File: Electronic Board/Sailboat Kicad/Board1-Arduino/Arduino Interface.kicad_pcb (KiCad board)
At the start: 2 copper layers, 69.9 x 101 mm, 51 parts, among them J1 Conn_01x02, J10 Conn_01x02, J11 Conn_01x03_Male, J12 Conn_01x03_Male, J13 Conn_01x03_Male, J14 Conn_01x03_Male, J15 Conn_01x04, J16 Conn_01x04, J17 Conn_01x04, J18 Conn_01x04, J19 Conn_01x03, J2 Conn_01x08, J20 Conn_01x03, J21 Conn_01x02, J22 Conn_01x02, J23 Conn_01x06, J24 Conn_01x03, J25 Conn_01x06, J26 Conn_02x02_Odd_Even, J3 Conn_01x08, J31 Conn_01x04, J32 Conn_01x04, J34 Conn_01x02, J35 Conn_01x02, J36 Conn_01x02, J37 Conn_01x02, J4 Conn_01x08, J5 Conn_02x18_Odd_Even, J6 Conn_01x08, J7 Conn_01x08, J8 Conn_01x08, J9 Conn_01x02, U1 L7805, U2 L7805, U3 L7805

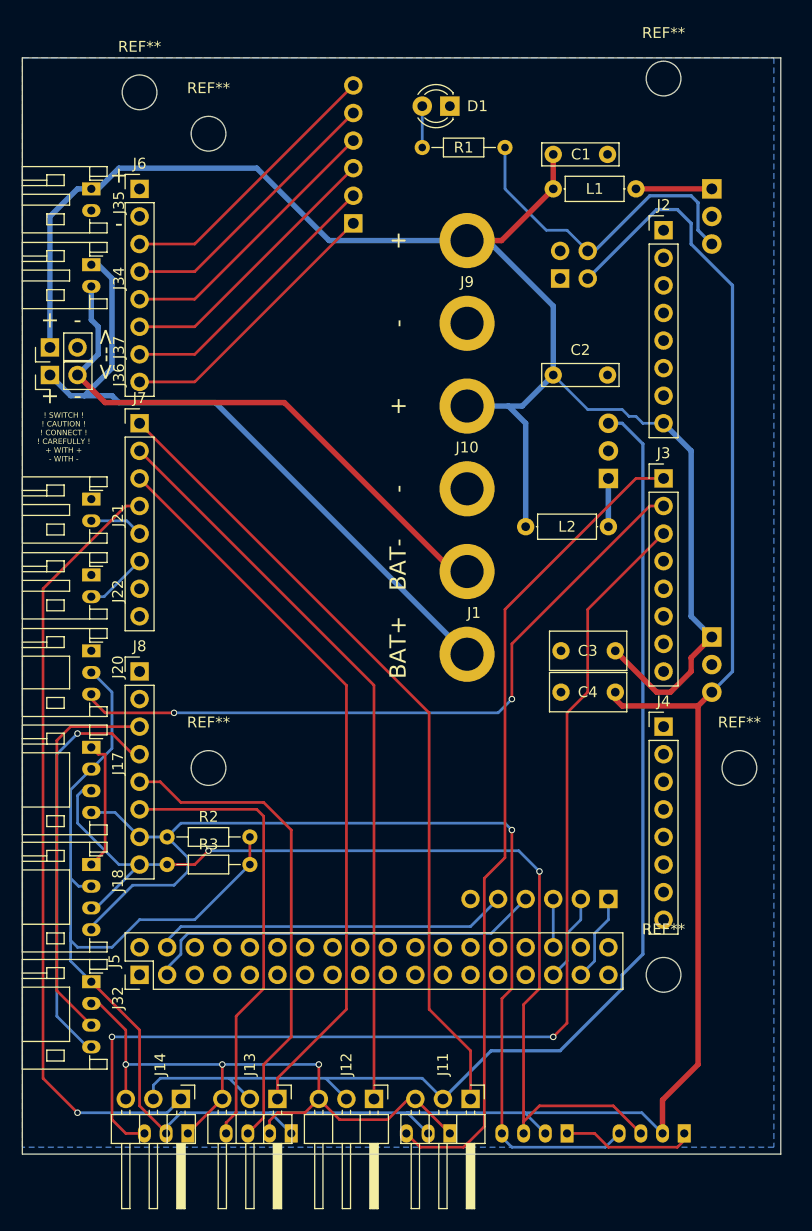
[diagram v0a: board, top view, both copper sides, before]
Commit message: Cleaned up, and added security, text and better usability, preparation for board v2
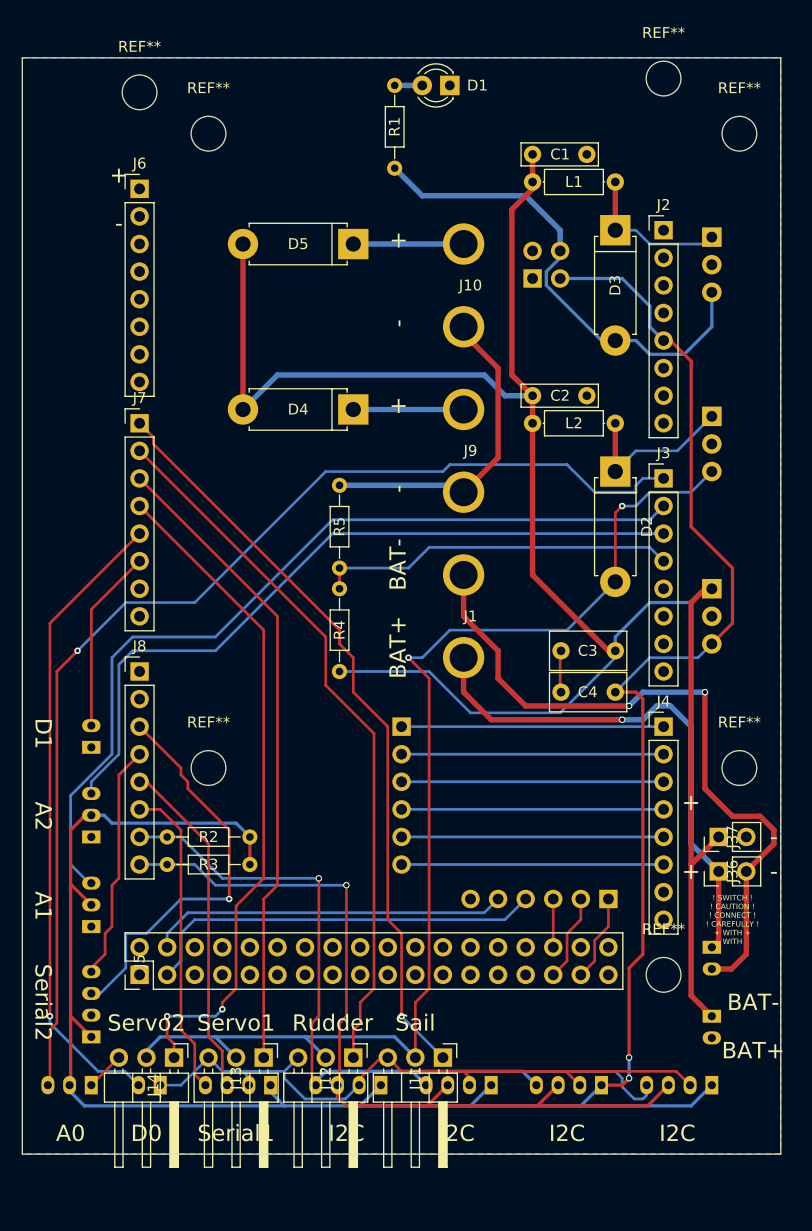
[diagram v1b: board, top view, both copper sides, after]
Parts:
- added D2: D_Schottky, Diodes_THT:D_5W_P10.16mm_Horizontal, F.Cu at (172.7, 90.8)
- added D3: D_Schottky, Diodes_THT:D_5W_P10.16mm_Horizontal, F.Cu at (172.7, 68.6)
- added D4: D_Schottky, Diodes_THT:D_5W_P10.16mm_Horizontal, F.Cu at (148.6, 85.1)
- added D5: D_Schottky, Diodes_THT:D_5W_P10.16mm_Horizontal, F.Cu at (148.6, 69.8)
- added R4: 20k, Resistors_THT:R_Axial_DIN0204_L3.6mm_D1.6mm_P7.62mm_Horizontal, F.Cu at (147.3, 109.2)
- added R5: 12k, Resistors_THT:R_Axial_DIN0204_L3.6mm_D1.6mm_P7.62mm_Horizontal, F.Cu at (147.3, 99.7)
- added REF**: MountingHole_3.2mm_M3, Mounting_Holes:MountingHole_3.2mm_M3, F.Cu at (184.2, 59.7)
- J17, J18, J20, J21, J22, J32, J34, J35: moved to B.Cu
- moved J35 95.3 mm to (181.6, 141.0)
- moved J34 85.0 mm to (181.6, 134.6)
- moved J36 76.7 mm to (182.2, 127.6)
- moved J37 76.3 mm to (182.2, 124.5)
- moved J17 65.1 mm to (181.6, 147.3), turned to 180 degrees
- moved J21 54.3 mm to (130.8, 147.3), turned to 180 degrees
- moved J23 46.6 mm to (153.0, 114.3), turned to 180 degrees
- moved J18 33.5 mm to (151.1, 147.3), turned to 180 degrees
- moved J19 33.3 mm to (124.5, 147.3)
- moved J24 28.7 mm to (124.5, 124.5), turned to 90 degrees
- moved J20 25.4 mm to (124.5, 132.7), turned to 90 degrees
- moved J22 15.9 mm to (124.5, 116.2), turned to 90 degrees
- moved J9 15.6 mm to (158.8, 88.9)
- moved J10 14.9 mm to (158.8, 73.7)
- moved U2 11.1 mm to (181.6, 85.7), turned to 270 degrees
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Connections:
- C4 pad 1: /Connectors/5V-Sensors -> /ArduinoMega/5V
- J10 pad 2: BAT+ -> Net-(D5-Pad1)
- J15 pad 1: GND -> /ArduinoMega/5V
- J15 pad 2: /Connectors/5V-Sensors -> GND
- J16 pad 1: GND -> /ArduinoMega/5V
- J16 pad 2: /Connectors/5V-Sensors -> GND
- J17 pad 1: GND -> /ArduinoMega/5V
- J17 pad 2: /Connectors/5V-Sensors -> GND
- J18 pad 1: GND -> /ArduinoMega/5V
- J18 pad 2: /Connectors/5V-Sensors -> GND
- J19 pad 2: /Connectors/5V-Sensors -> /ArduinoMega/5V
- J2 pad 8: BAT+ -> /ArduinoMega/Vin
- J20 pad 2: /Connectors/5V-Sensors -> /ArduinoMega/5V
- J24 pad 2: /Connectors/5V-Sensors -> /ArduinoMega/5V
- J26 pad 2: /Connectors/5V-Sensors -> /ArduinoMega/5V
- J31 pad 1: /Connectors/5V-Sensors -> /ArduinoMega/5V
- J32 pad 1: /Connectors/5V-Sensors -> /ArduinoMega/5V
- J4 pad 1: /ArduinoMega/A8 -> RC1
- J4 pad 2: /ArduinoMega/A9 -> RC2
- J4 pad 3: /ArduinoMega/A10 -> RC3
- J4 pad 4: /ArduinoMega/A11 -> RC4
- J4 pad 5: /ArduinoMega/A12 -> RC5
- J4 pad 6: /ArduinoMega/A13 -> RC6
- J6 pad 3: RC6 -> /ArduinoMega/13
- J6 pad 4: RC5 -> /ArduinoMega/12
- J6 pad 5: RC4 -> /ArduinoMega/11
- J6 pad 6: RC3 -> /ArduinoMega/10
- J6 pad 7: RC2 -> /ArduinoMega/9
- J6 pad 8: RC1 -> /ArduinoMega/8
- J9 pad 2: BAT+ -> Net-(D4-Pad1)
- R2 pad 2: /Connectors/5V-Sensors -> /ArduinoMega/5V
- R3 pad 2: /Connectors/5V-Sensors -> /ArduinoMega/5V
- U3 pad 3: /Connectors/5V-Sensors -> /ArduinoMega/5V
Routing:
- net /Connectors/5V-Sensors: track 239.0 -> 0.00 mm
- net /ArduinoMega/5V: track 0.00 -> 217.5 mm, vias 0 -> 2
- net D0: track 4.93 -> 59.6 mm, vias 0 -> 1
- net A2: track 102.8 -> 68.1 mm, vias 2 -> 0
- net /ArduinoMega/A3: track 0.00 -> 33.1 mm
- net BAT+: track 152.7 -> 180.8 mm
- net A0: track 76.5 -> 104.3 mm, vias 0 -> 1
- net SDA: track 96.1 -> 74.9 mm
- net SCL: track 93.4 -> 77.1 mm, vias 2 -> 1
- net RX_2: track 38.0 -> 21.9 mm, vias 1 -> 0
- net Net-(J1-Pad1): track 63.3 -> 48.1 mm, vias 0 -> 1
- net A1: track 64.7 -> 79.8 mm, vias 2 -> 0
- net /Connectors/5V-Rpi: track 30.7 -> 45.3 mm
- net TX_1: track 45.6 -> 31.7 mm
- net RX_1: track 42.3 -> 29.0 mm
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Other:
- board text added: "A0"
- board text added: "A1"
- board text added: "A2"
- board text added: "D0"
- board text added: "D1"
- board text added: "I2C"
- board text added: "RPi-5V"
- board text added: "Rudder"
- board text added: "Sail"
- board text added: "Sensors-5V"
- board text added: "Serial1"
- board text added: "Serial2"
- board text added: "Servo-5V"
- board text added: "Servo1"
- board text added: "Servo2"
- board text removed: "<-->"
